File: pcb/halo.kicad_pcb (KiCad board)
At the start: 4 copper layers, 23.4 x 23.3 mm, 167 parts, among them U1 STM8L151G6

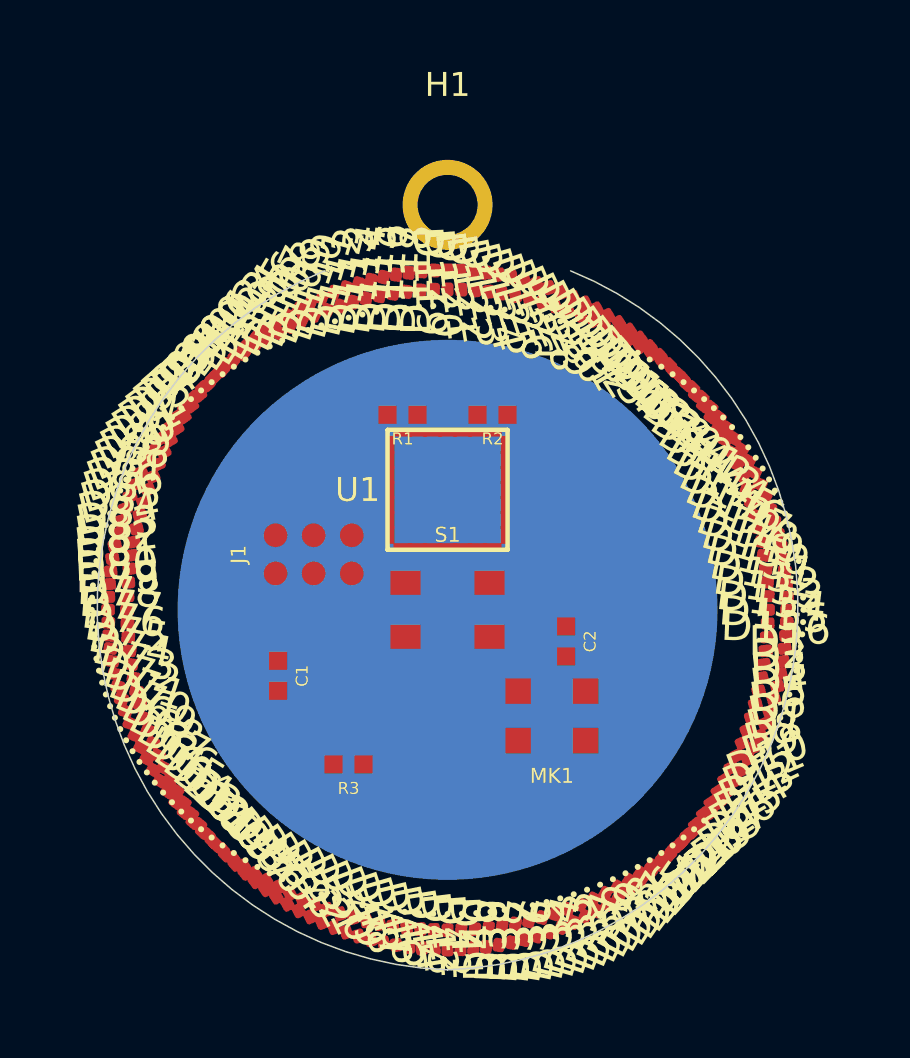
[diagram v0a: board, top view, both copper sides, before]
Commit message: Fix radial placement orientation to invert rotation parity correctly
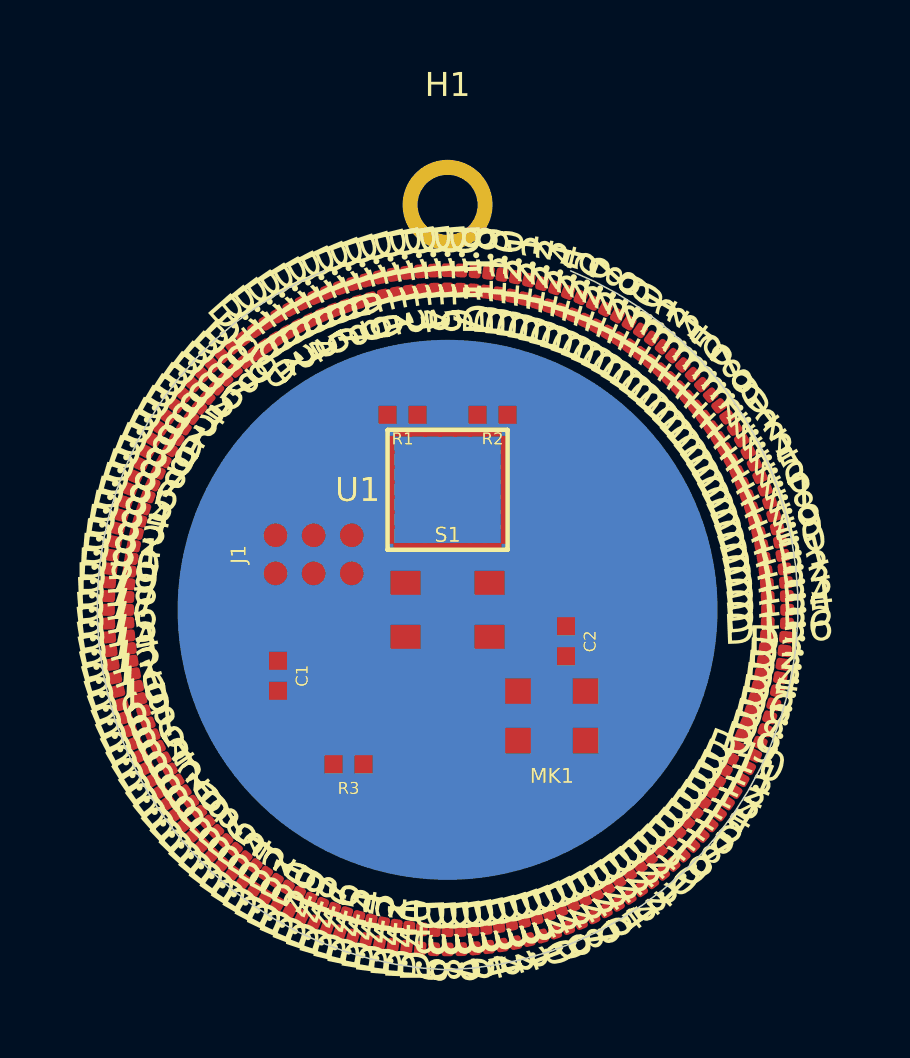
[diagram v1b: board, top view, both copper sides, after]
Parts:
- turned D10 to 159.231 degrees
- turned D100 to -48.4615 degrees
- turned D101 to -50.7692 degrees
- turned D102 to -53.0769 degrees
- turned D103 to -55.3846 degrees
- turned D104 to -57.6923 degrees
- turned D105 to -60 degrees
- turned D106 to -62.3077 degrees
- turned D107 to -64.6154 degrees
- turned D108 to -66.9231 degrees
- turned D109 to -69.2308 degrees
- turned D11 to 156.923 degrees
- turned D110 to -71.5385 degrees
- turned D111 to -73.8462 degrees
- turned D112 to -76.1538 degrees
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
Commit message: Update constraints to 4-layer 0.09mm, patch ERC pad types, resolve LED radial collisions by slimming pads to 0.28mm width, fix MCU absolute rotation logic
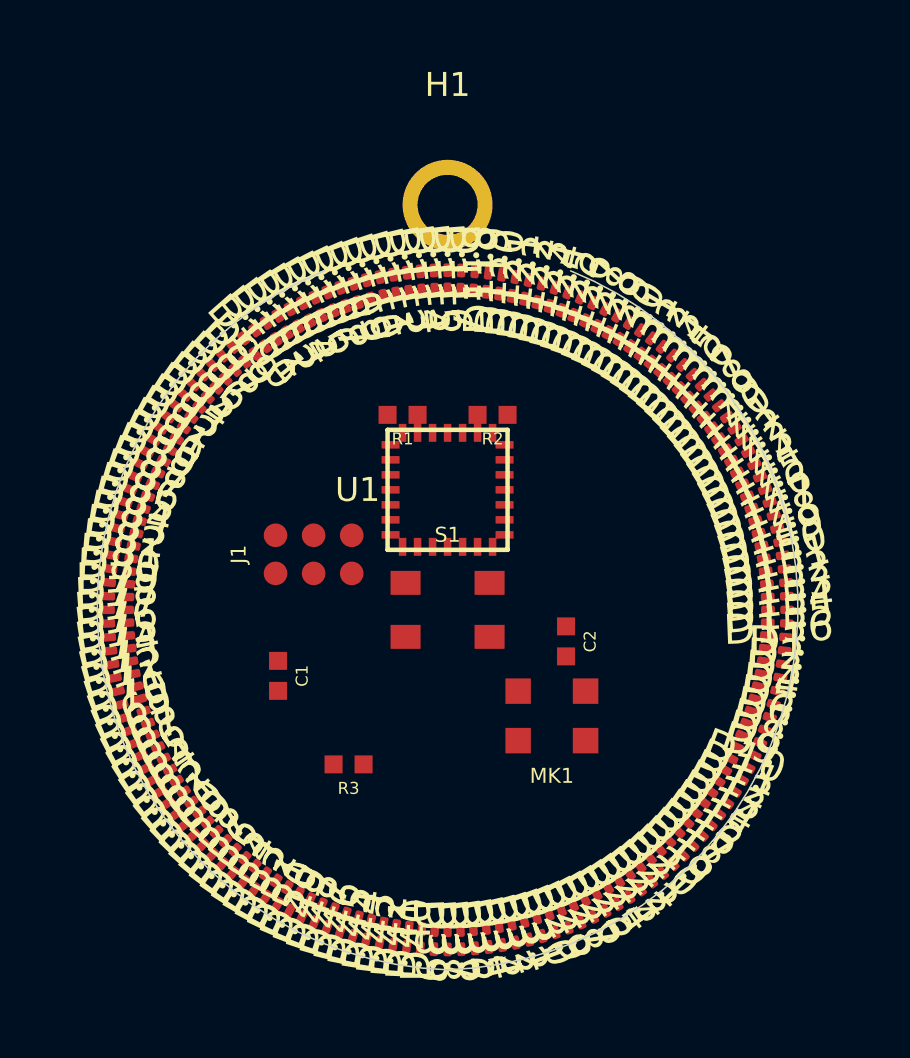
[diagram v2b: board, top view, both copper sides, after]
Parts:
- removed BT1: , BAT-HLD-001:BAT-HLD-001-HALO
